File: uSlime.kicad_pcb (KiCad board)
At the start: 2 copper layers, 21.9 x 27.5 mm, 25 parts, among them J1 USB_B_Micro, U1 ESP32-C6-MINI-1, U2 S2B-PH-K-S-GW, U3 AP2112K-3.3TRG1, U4 MCP73831T-2ACI/OT, U5 BNO085, U6 MSK-12C02_SMD_SPDT_SWITCH, Y1 32.768

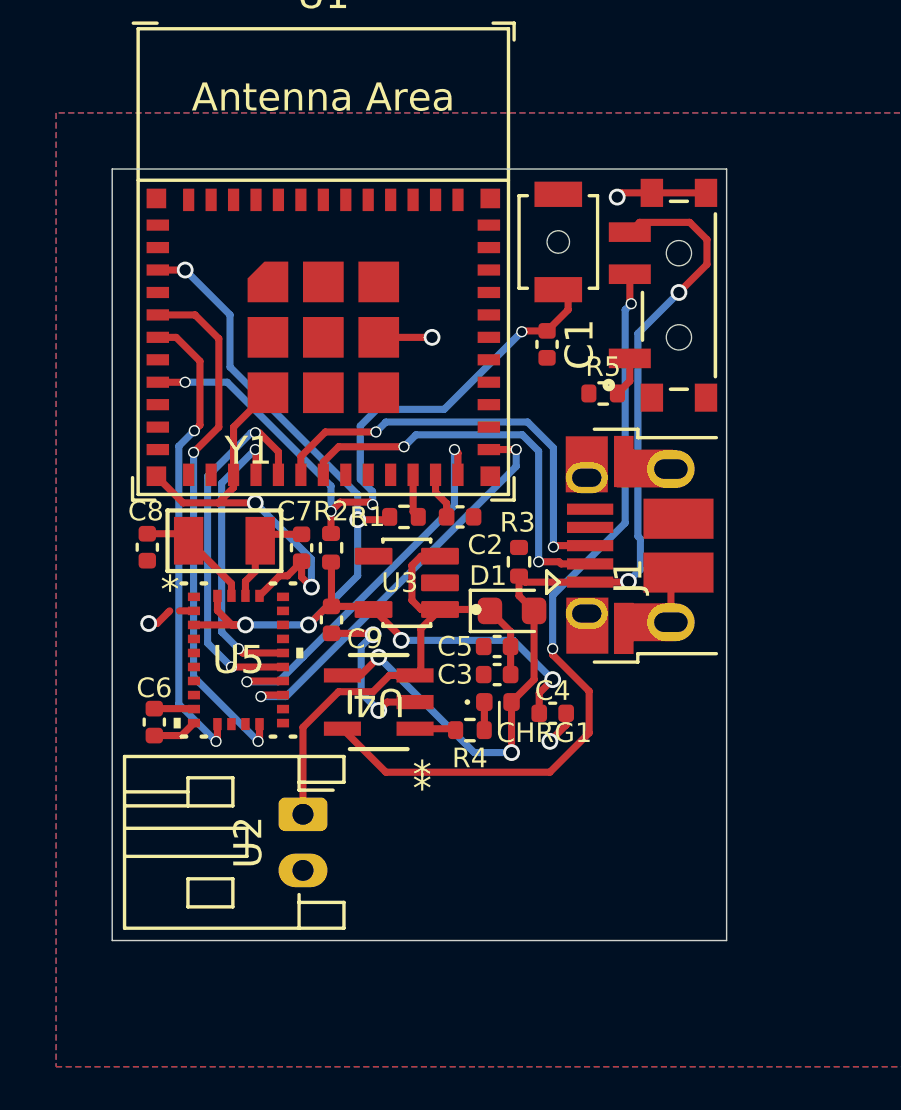
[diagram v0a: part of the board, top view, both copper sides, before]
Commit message: Add connector for testing
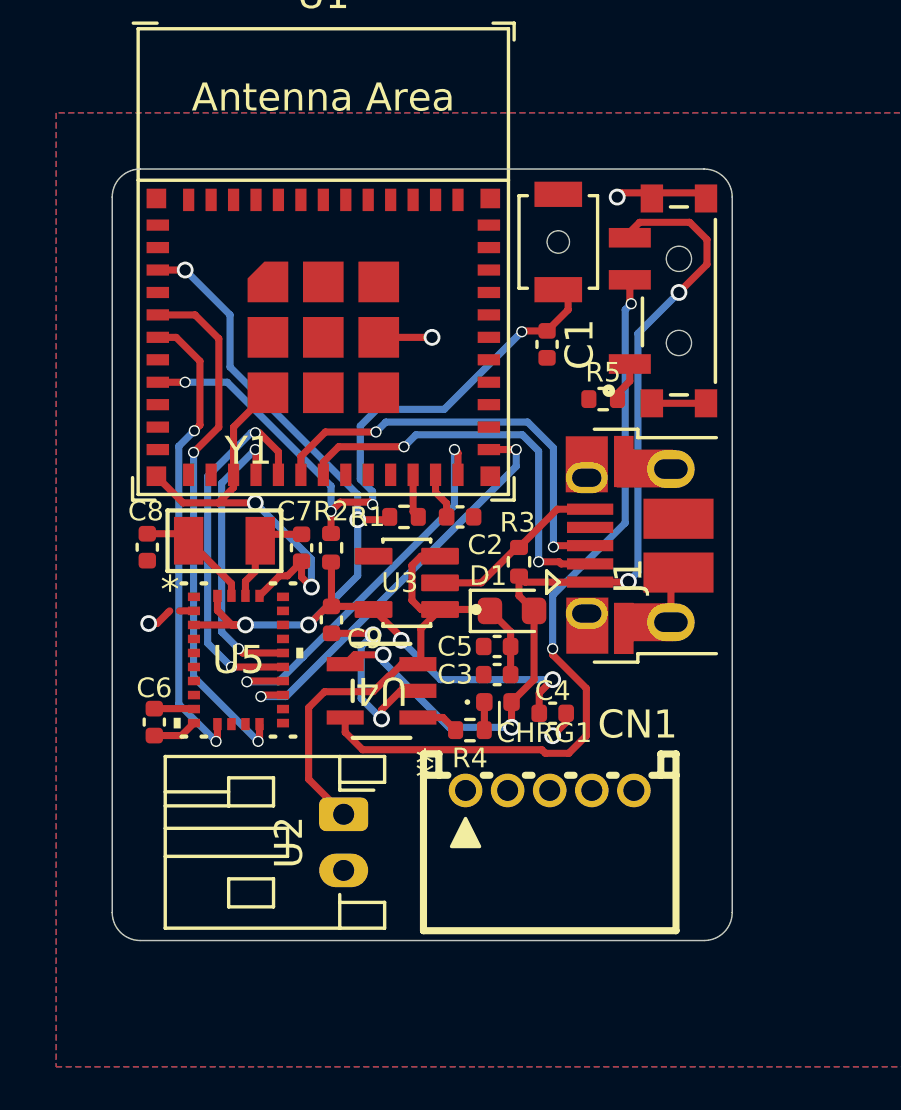
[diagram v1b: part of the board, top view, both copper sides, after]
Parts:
- added CN1: X1502WR-05K-N0SN, uSlime-libs:CONN-TH_5P-P1.50_X1502WR-05K-N0SN, F.Cu at (116.2, 111.5)
- moved U2 1.45 mm to (108.9, 112.3)
- moved U4 0.41 mm to (110.2, 108.0)
- moved R5 0.20 mm to (118.2, 97.5)
- moved U6 0.20 mm to (120.8, 94.0)
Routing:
- net GND: track 32.8 -> 41.8 mm
- net VBUS: track 35.1 -> 33.7 mm
- net VBAT: track 18.5 -> 19.0 mm
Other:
- board size 21.9 x 27.5 mm -> 22.1 x 27.5 mm

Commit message: Add fiducial
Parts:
- added REF**: Fiducial_0.5mm_Mask1mm, Fiducial:Fiducial_0.5mm_Mask1mm, F.Cu at (119.5, 115.5)
- added REF**: Fiducial_0.5mm_Mask1mm, Fiducial:Fiducial_0.5mm_Mask1mm, F.Cu at (103.7, 115.5)
- added REF**: Fiducial_0.5mm_Mask1mm, Fiducial:Fiducial_0.5mm_Mask1mm, F.Cu at (115.8, 97.7)

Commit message: Create prelim PCB
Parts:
- removed U2: S2B-PH-K-S-GW, Connector_JST:JST_PH_S2B-PH-K_1x02_P2.00mm_Horizontal
- added ?: , , F.Cu at (103.5, 92.3)
- added ?: , , F.Cu at (125.4, 113.4)
- added CN2: 1.25T-2AW, uSlime-libs:CONN-TH_2P-P1.25_1.25T-2AW, F.Cu at (110.8, 113.3)
- added D2: D, Diode_SMD:D_0402_1005Metric, F.Cu at (113.5, 108.8)
- added R6: 5.1k, Resistor_SMD:R_0402_1005Metric, F.Cu at (122.0, 98.8)
- added R7: 5.1k, Resistor_SMD:R_0402_1005Metric, F.Cu at (123.8, 98.8)
- C1, C2: value 0.1UF-0603-25V-(+80/-20%) -> 0.1uF
- D1: footprint Diode_SMD:D_0603_1608Metric -> Diode_SMD:D_0402_1005Metric
- J1: value USB_B_Micro -> USB_C_Receptacle_USB2.0_14P; footprint Connector_USB:USB_Micro-B_Amphenol_10103594-0001LF_Horizontal -> Connector_USB:USB_C_Receptacle_GCT_USB4105-xx-A_16P_TopMnt_Horizontal
- R3: value 100K -> 180k
- moved R2 14.9 mm to (121.3, 95.3)
- moved REF** 12.5 mm to (126.2, 104.7)
- moved C2 9.21 mm to (120.8, 96.8)
- moved U4 7.50 mm to (117.8, 107.9), turned to -90 degrees
- moved C5 7.13 mm to (112.4, 113.2), turned to 90 degrees
- moved R4 6.79 mm to (118.7, 105.2), turned to 0 degrees
- moved R3 6.10 mm to (112.5, 108.8)
- moved CHRG1 6.04 mm to (118.7, 104.2)
- moved C4 5.84 mm to (112.1, 104.8), turned to 90 degrees
- moved U6 5.60 mm to (126.5, 94.2)
- moved J1 5.34 mm to (124.5, 104.6)
- moved R5 5.00 mm to (123.2, 97.3), turned to 90 degrees
- moved RESET1 5.00 mm to (121.5, 92.0)
- moved REF** 4.89 mm to (108.2, 113.7)
- moved C8 4.85 mm to (106.8, 102.7)
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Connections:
- C3 pad 1: VBAT -> Net-(D1-K)
- CN1 pad 1: unconnected-(CN1-Pad1) -> BNO_SDA
- CN1 pad 2: unconnected-(CN1-Pad2) -> +3.3V
- CN1 pad 3: unconnected-(CN1-Pad3) -> BNO_INT2
- CN1 pad 4: unconnected-(CN1-Pad4) -> GND
- CN1 pad 5: unconnected-(CN1-Pad5) -> BNO_SCL
- D1 pad 1: VBAT -> Net-(D1-K)
- R3 pad 1: VBUS -> VBAT
- R3 pad 2: GND -> BatSense
- U1 pad 12: /ESP32-C6FH4/IO0 -> BatSense
- U1 pad 13: /ESP32-C6FH4/IO1/V_BATT_2 -> BNO_INT
- U1 pad 24: BNO_CS -> /ESP32-C6FH4/IO18/~{CS}
- U1 pad 25: BNO_MOSI -> /ESP32-C6FH4/IO19/SCK
- U1 pad 5: BNO_INT -> BNO_INT2
- U1 pad 6: BNO_RST -> /ESP32-C6FH4/IO3
- U3 pad 1: VBAT -> Net-(D1-K)
- U3 pad 3: VBAT -> Net-(D1-K)
- U5 pad 11: BNO_RST -> unconnected-(U5-NRST-Pad11)
- U5 pad 17: BNO_MOSI -> unconnected-(U5-SA0/H_MOSI-Pad17)
- U5 pad 18: BNO_CS -> unconnected-(U5-H_CSN-Pad18)
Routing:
- net BNO_INT2: track 0.00 -> 27.5 mm, vias 0 -> 1
- net +3.3V: track 37.0 -> 60.3 mm
- net BNO_RST: track 16.9 -> 0.00 mm, vias 2 -> 0
- net BatSense: track 0.00 -> 16.9 mm, vias 0 -> 2
- net BNO_MOSI: track 14.9 -> 0.00 mm, vias 2 -> 0
- net BNO_CS: track 14.3 -> 0.00 mm, vias 2 -> 0
- net BNO_SCL: track 13.3 -> 24.9 mm
- net Net-(J1-CC1): track 0.00 -> 9.48 mm
- net GND: track 41.8 -> 51.1 mm, vias 8 -> 2
- net BNO_INT: track 18.8 -> 9.74 mm
- net Net-(J1-CC2): track 0.00 -> 6.85 mm
- net VBUS: track 33.7 -> 27.7 mm, vias 4 -> 2
- net BNO_SDA: track 10.4 -> 16.1 mm
- net VBAT: track 19.0 -> 14.0 mm, vias 0 -> 2
- net /ESP32-C6FH4/IO9/BOOT: track 1.66 -> 6.51 mm, vias 0 -> 2
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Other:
- board size 22.1 x 27.5 mm -> 27.8 x 27.5 mm

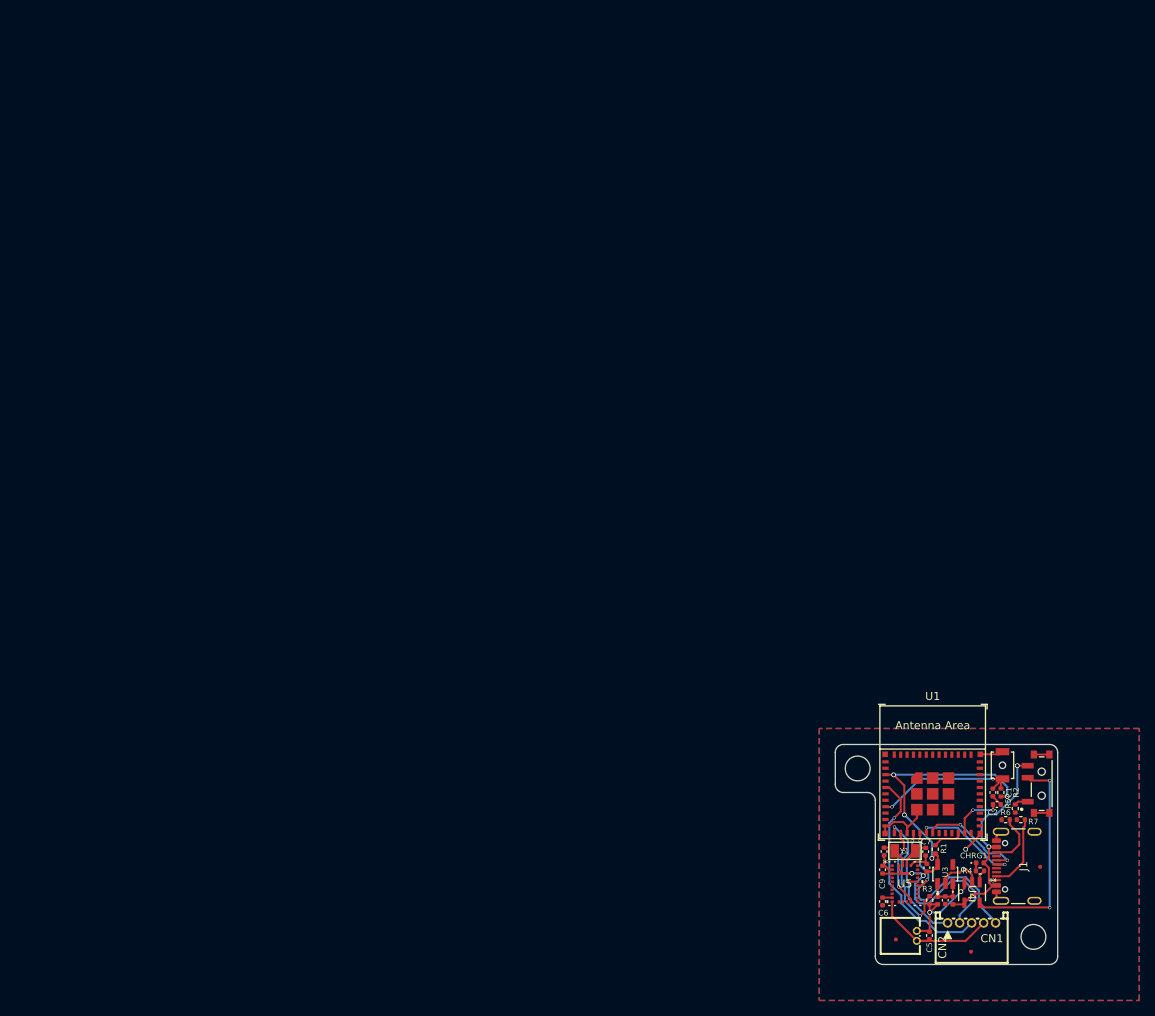
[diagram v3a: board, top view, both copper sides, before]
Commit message: Add status LED
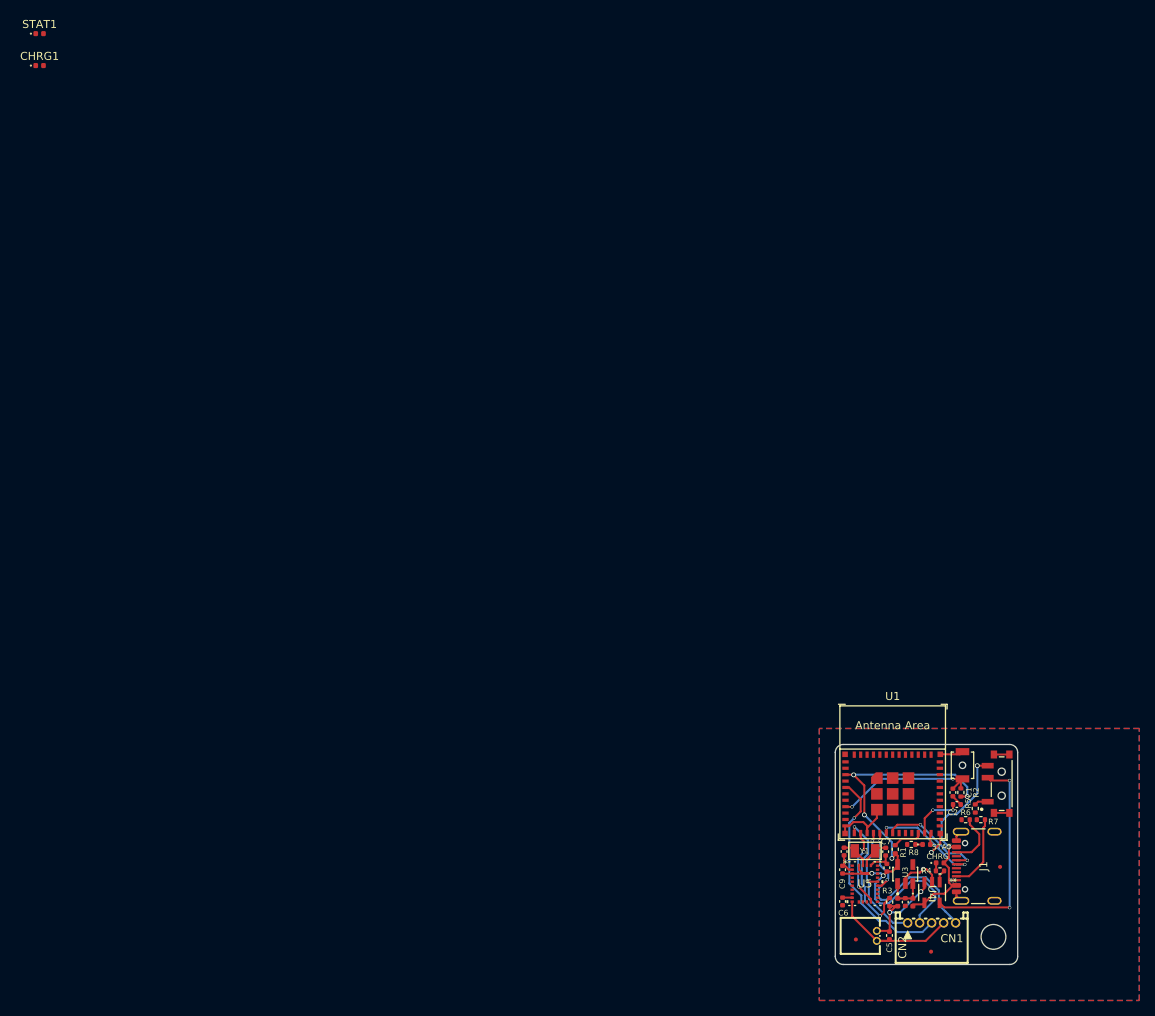
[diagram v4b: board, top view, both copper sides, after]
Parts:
- removed the ? at (103.5, 92.3)
- added CHRG1: LED, LED_SMD:LED_0402_1005Metric, F.Cu at (1.19, 4.49)
- added R8: 1k, Resistor_SMD:R_0402_1005Metric, F.Cu at (110.2, 101.8)
- added STAT: LED, LED_SMD:LED_0402_1005Metric, F.Cu at (112.0, 101.8)
- added STAT1: LED, LED_SMD:LED_0402_1005Metric, F.Cu at (1.19, 0.49)
- moved C3 5.01 mm to (109.4, 109.0)
- moved D1 5.01 mm to (110.3, 109.1)
- moved D2 5.01 mm to (108.5, 109.1)
- moved R3 5.01 mm to (107.5, 109.0)
- moved ? 5.00 mm to (120.4, 113.4)
- moved C1 5.00 mm to (115.3, 95.3)
- moved C2 5.00 mm to (115.8, 96.8)
- moved C4 5.00 mm to (107.1, 104.8)
- moved C5 5.00 mm to (107.4, 113.2)
- moved C6 5.00 mm to (101.6, 109.0)
- moved C7 5.00 mm to (107.0, 102.8)
- moved C8 5.00 mm to (101.8, 102.7)
- moved C9 5.00 mm to (101.6, 105.0)
- moved CHRG 5.00 mm to (113.7, 104.2)
- moved CN1 5.00 mm to (112.7, 111.7)
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- renumbered CHRG1 to CHRG
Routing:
- net /ESP32-C6FH4/IO18/~{CS}: track 0.00 -> 1.46 mm
- net Net-(STAT1-K): track 0.00 -> 0.91 mm
- net Net-(D1-K): track 4.79 -> 5.43 mm
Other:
- board size 27.8 x 27.5 mm -> 22.8 x 27.5 mm

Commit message: 2nd version but smaller at 25x28
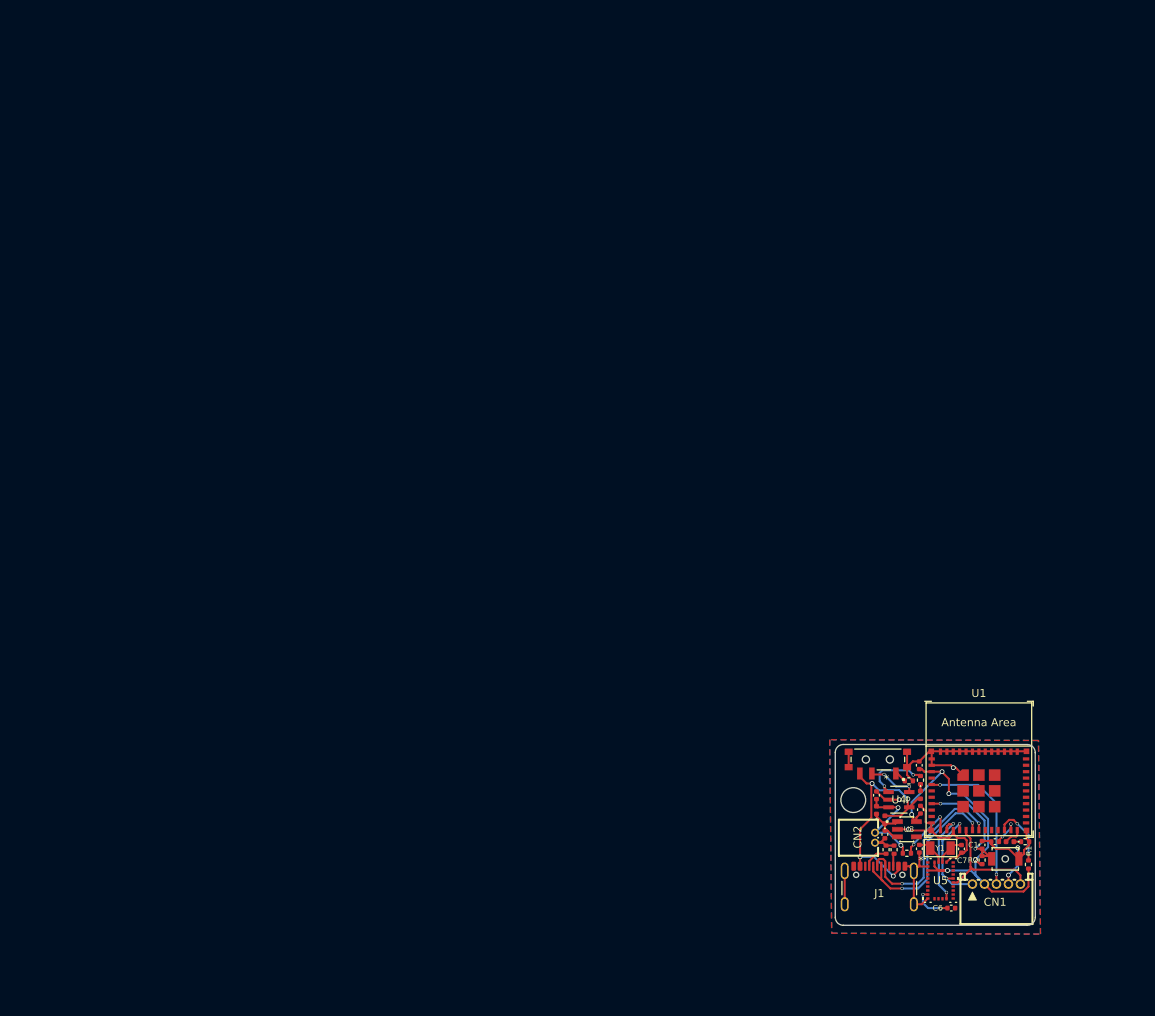
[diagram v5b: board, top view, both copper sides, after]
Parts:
- removed CHRG1, STAT1: LED, LED_SMD:LED_0402_1005Metric
- removed REF** (x3): Fiducial_0.5mm_Mask1mm, Fiducial:Fiducial_0.5mm_Mask1mm
- moved ? 24.5 mm to (102.9, 96.3)
- moved C5 17.6 mm to (105.8, 95.7), turned to -90 degrees
- moved R1 16.8 mm to (124.8, 104.3)
- moved C9 16.2 mm to (111.2, 92.0)
- moved U6 15.8 mm to (106.0, 91.2), turned to 180 degrees
- moved R8 14.2 mm to (124.4, 101.5), turned to 180 degrees
- moved J1 13.8 mm to (106.2, 108.2), turned to 0 degrees
- moved C6 13.6 mm to (115.2, 109.8), turned to 180 degrees
- moved RESET 12.9 mm to (121.9, 103.7), turned to 180 degrees
- moved R7 12.4 mm to (107.0, 102.5), turned to -90 degrees
- moved U4 12.3 mm to (108.6, 96.2), turned to 0 degrees
- moved CN2 12.3 mm to (105.6, 101.0)
- moved D2 11.8 mm to (105.8, 97.5), turned to 90 degrees
- moved R4 11.6 mm to (111.3, 93.8), turned to 90 degrees
- moved D1 10.9 mm to (106.8, 98.8), turned to 90 degrees
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- renumbered RESET1 to RESET
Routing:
- net GND: track 51.2 -> 86.3 mm, vias 2 -> 5
- net Net-(U4-PROG): track 27.8 -> 6.05 mm
- net D+ P: track 13.3 -> 24.1 mm
- net D- N: track 13.5 -> 23.9 mm
- net +3.3V: track 60.3 -> 50.4 mm, vias 6 -> 5
- net BNO_SCL: track 24.9 -> 15.8 mm, vias 2 -> 0
- net BatSense: track 16.7 -> 7.73 mm
- net BNO_INT2: track 27.5 -> 19.2 mm, vias 1 -> 2
- net Net-(U4-STAT): track 1.64 -> 8.39 mm, vias 0 -> 2
- net Net-(J1-CC1): track 9.48 -> 3.12 mm
- net Net-(J1-CC2): track 6.85 -> 1.60 mm
- net /ESP32-C6FH4/IO8: track 3.77 -> 7.90 mm, vias 0 -> 2
- net VBUS: track 27.7 -> 31.6 mm, vias 2 -> 4
- net Net-(U5-CAP): track 1.20 -> 5.00 mm, vias 0 -> 2
- net /ESP32-C6FH4/IO9/BOOT: track 6.51 -> 3.57 mm
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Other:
- board size 22.8 x 27.5 mm -> 25 x 22.6 mm

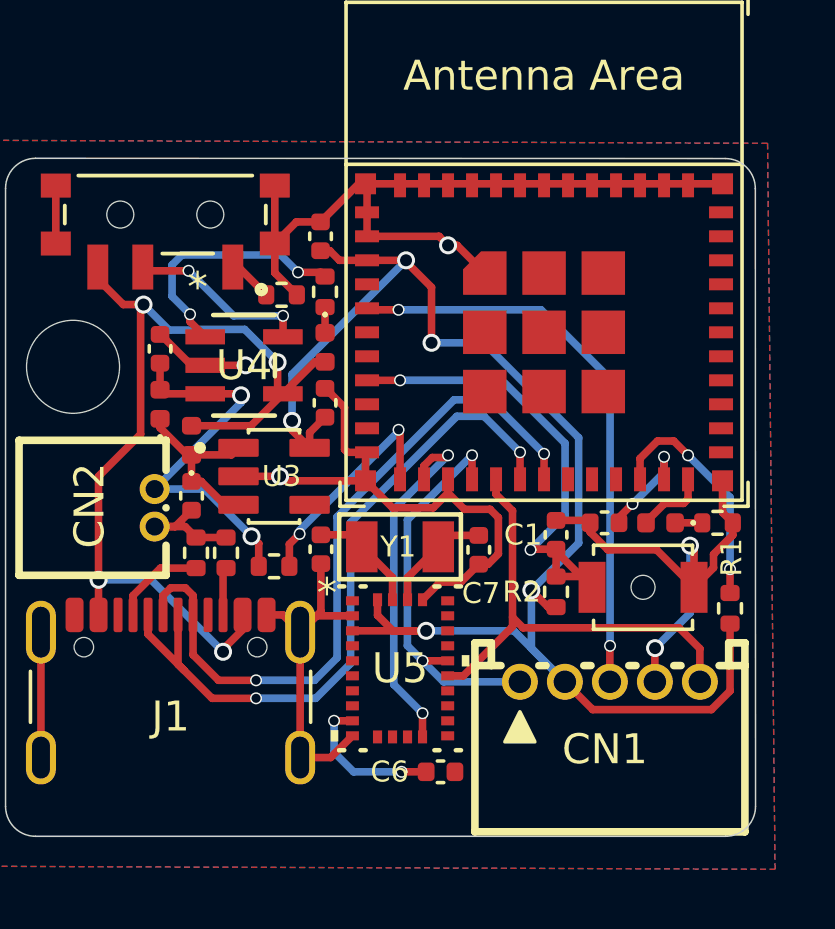
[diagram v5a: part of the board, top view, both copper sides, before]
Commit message: Fix some DRC and generate gerber
Some errors popped up on annular diameter, fixed and generated gerber
files for production
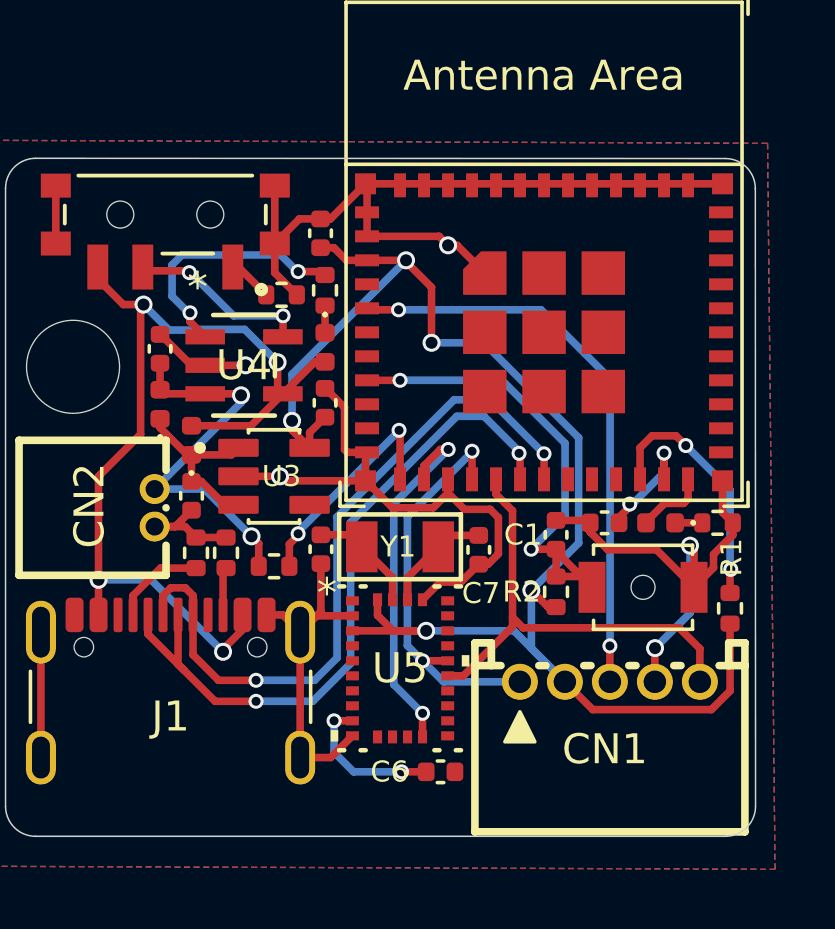
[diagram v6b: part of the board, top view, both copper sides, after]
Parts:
- moved C9 0.10 mm to (111.2, 91.8)
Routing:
- net /ESP32-C6FH4/IO8: track 7.90 -> 8.43 mm
